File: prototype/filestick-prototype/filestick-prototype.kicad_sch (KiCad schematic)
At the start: 50 parts, among them U2 LMV324

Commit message: add GPIO headers etc
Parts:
- removed J?: Conn_01x07_Male, symbol Connector:Conn_01x07_Male
- added J3: GPIO header 1, symbol Connector:Conn_01x09_Male
- added J5: GPIO header 2, symbol Connector:Conn_01x16_Male
- added J6: SPI header, symbol Connector:Conn_01x10_Male
- added TP2: Econet TP header, symbol Connector:Conn_01x12_Male
- J4: renamed from J?; value Conn_01x05_Male -> UART header
- gave numbers to parts that had none: 47
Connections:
- net +3.3V: now also J3.1 (Pin_1), J5.16 (Pin_16), J6.10 (Pin_10), TP2.1 (Pin_1)
- net COLLISION_DETECT: now also TP2.2 (Pin_2)
- net COLLISION_REF_PWM: now also TP2.4 (Pin_4)
- net ECONET_CLKEN: now also TP2.10 (Pin_10)
- net ECONET_CLKIO: now also TP2.6 (Pin_6)
- net ECONET_RXD: now also TP2.7 (Pin_7)
- net ECONET_TXD: now also TP2.8 (Pin_8)
- net ECONET_TXEN: now also TP2.9 (Pin_9)
- net GND: now also J3.9 (Pin_9), J5.1 (Pin_1), J6.1 (Pin_1), TP2.12 (Pin_12)
- net TERM_EN: now also TP2.3 (Pin_3)
- net at U4.11 (GPIO23): now also J3.7 (Pin_7)
- net at U4.12 (GPIO25): now also J3.8 (Pin_8)
- net at U4.18 (GPIO37_G1): now also TP2.5 (Pin_5)
- net at U4.2 (VIO): now also J3.2 (Pin_2)
- net at U4.24 (GPIO28): now also TP2.11 (Pin_11)
- net at U4.25 (GPIO2): now also J5.2 (Pin_2)
- net at U4.26 (GPIO46): now also J5.3 (Pin_3)
- net at U4.27 (GPIO47): now also J5.4 (Pin_4)
- net at U4.28 (GPIO45): now also J5.5 (Pin_5)
- net at U4.29 (GPIO48): now also J5.6 (Pin_6)
- net at U4.30 (GPIO3): now also J5.7 (Pin_7)
- net at U4.31 (GPIO4): now also J5.8 (Pin_8)
- net at U4.32 (GPIO44_G6): now also J5.9 (Pin_9)
- net at U4.33 (GPIO6): now also J5.10 (Pin_10)
- net at U4.34 (GPIO9): now also J5.11 (Pin_11)
- net at U4.35 (GPIO11): now also J5.12 (Pin_12)
- net at U4.36 (GPIO18): now also J5.13 (Pin_13)
- net at U4.37 (GPIO19): now also J5.14 (Pin_14)
- net SD_CD: now reaches R17.2, U4.38 (GPIO13), U5.7 (CD)
- net SD_CD: now also J6.2 (Pin_2)
- net SS3: now reaches U4.39 (GPIO21_SS3)
- net SS3: now also J6.3 (Pin_3)
- net at U4.4 (CDONE): now also J3.3 (Pin_3)
- net SS2: now reaches U4.40 (GPIO12_SS2)
- net SS2: now also J6.4 (Pin_4)
- net SD_SS: now reaches U4.43 (GPIO10_SS1), U5.6 (/CS)
- net SD_SS: now also J6.5 (Pin_5)
- net GPIO_20: now reaches U4.44 (GPIO20_G3)
- net GPIO_20: now also J5.15 (Pin_15)
- net MOSI: now reaches U4.45 (GPIO14_MOSI), U5.3 (DI)
- net MOSI: now also J6.6 (Pin_6)
- net MISO: now reaches U4.46 (GPIO17_MISO), U5.4 (DO)
- net MISO: now also J6.7 (Pin_7)
- net SCK: now reaches U4.47 (GPIO15_SCK), U5.5 (SCLK)
- net SCK: now also J6.8 (Pin_8)
- net FLASH_SS: now reaches U4.48 (GPIO16_SS0)
- net FLASH_SS: now also J6.9 (Pin_9)
- net at U4.5 (GPIO41_RGB2): now also J3.4 (Pin_4)
- net at U4.6 (GPIO39_RGB0): now also J3.5 (Pin_5)
- net at U4.7 (GPIO40_RGB1): now also J3.6 (Pin_6)

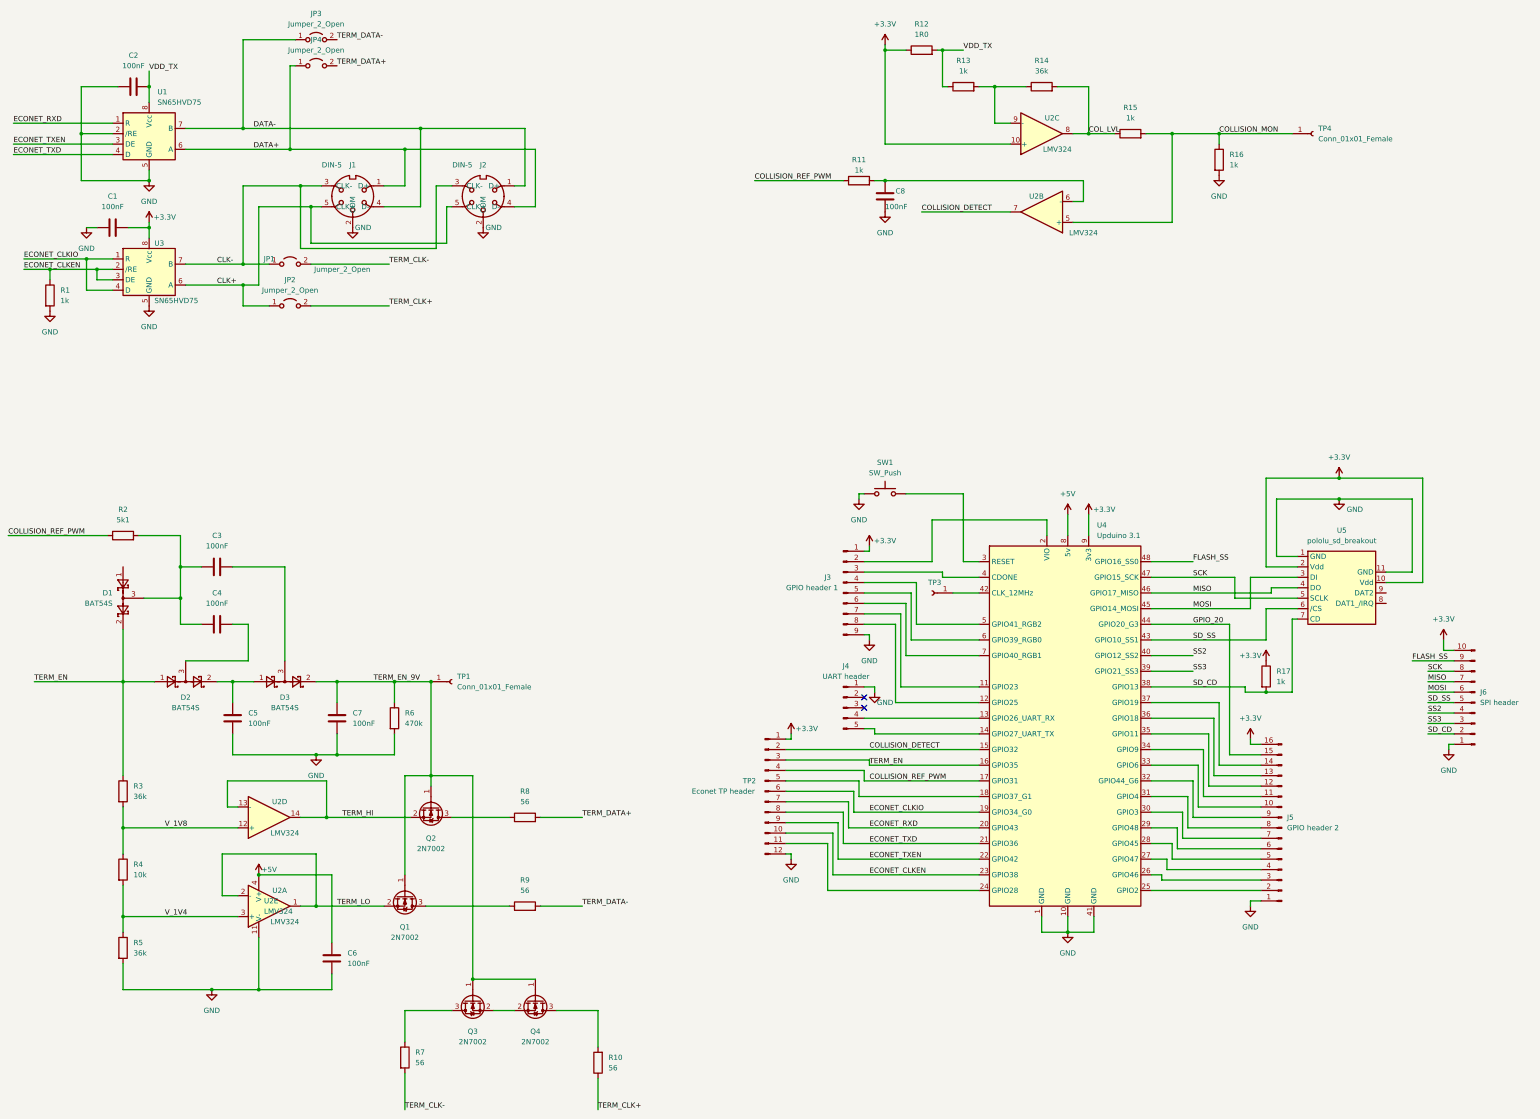
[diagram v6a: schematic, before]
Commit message: add annotations and footprints
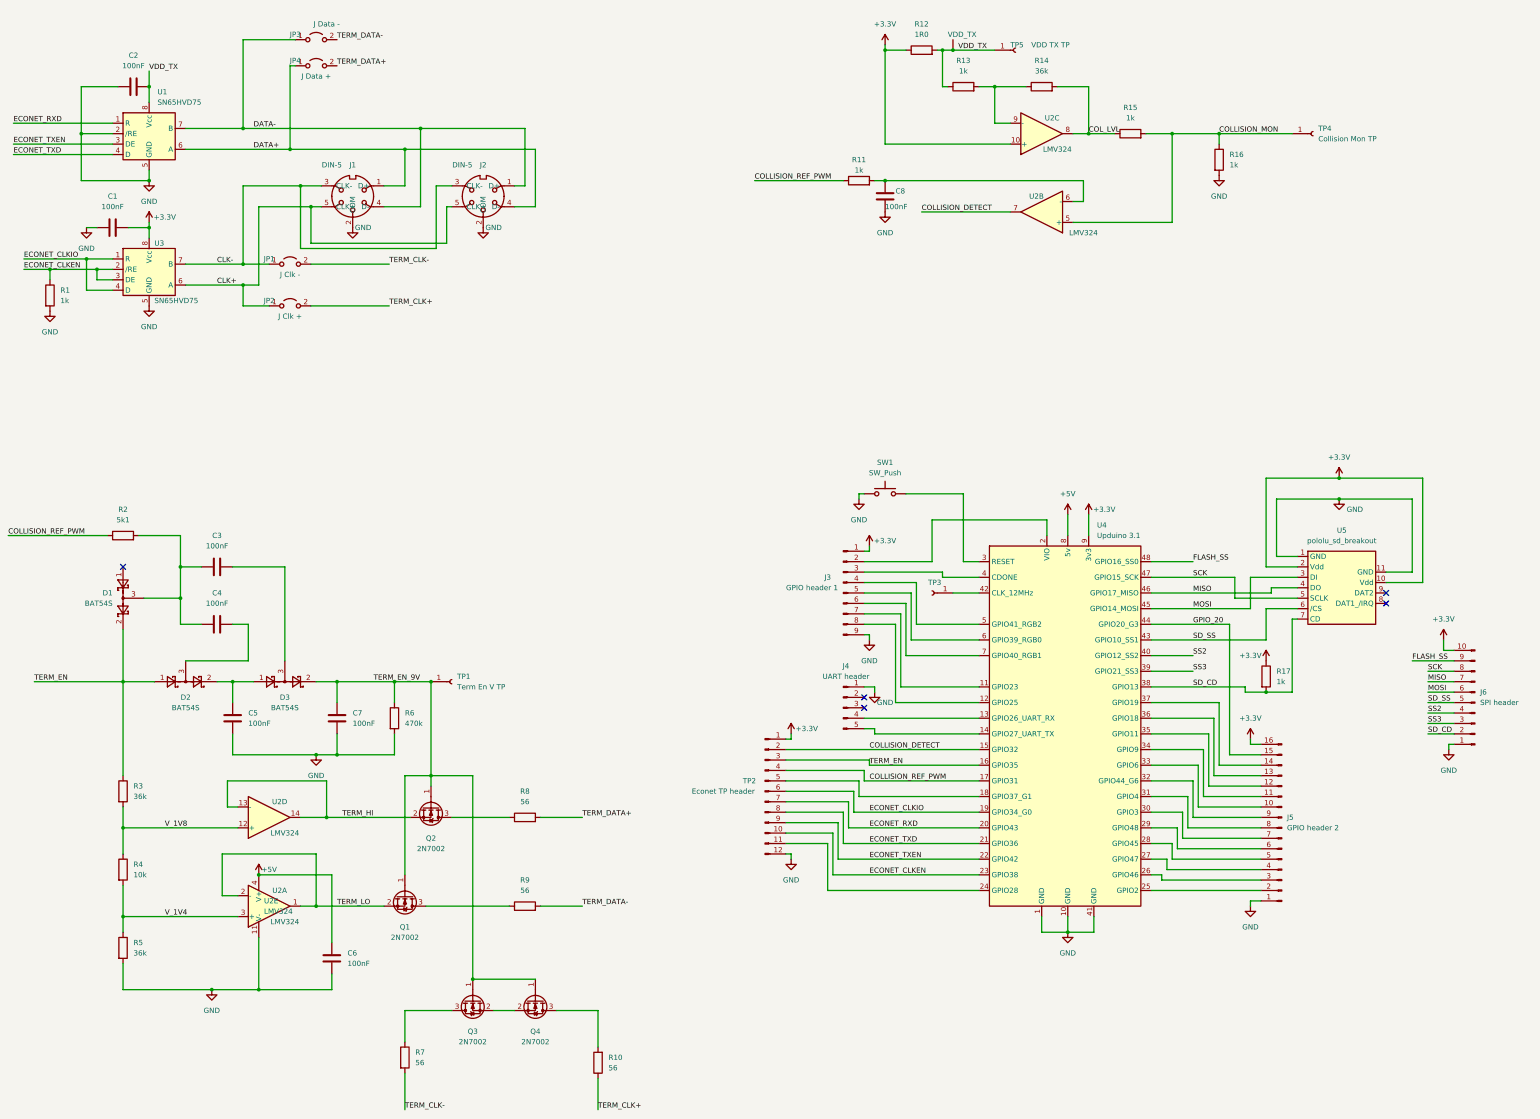
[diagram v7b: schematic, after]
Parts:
- added TP5: VDD TX TP, Connector_PinHeader_2.54mm:PinHeader_1x01_P2.54mm_Vertical, symbol Connector:Conn_01x01_Female
- C1, C2, C3, C4, C5, C6, C7, C8: footprint (none) -> Capacitor_SMD:C_0603_1608Metric_Pad1.08x0.95mm_HandSolder
- J1, J2: footprint (none) -> filestick-footprints:Lumberg_DIN41524_5pin
- J3: footprint (none) -> Connector_PinHeader_2.54mm:PinHeader_1x09_P2.54mm_Vertical
- J4: footprint (none) -> Connector_PinHeader_2.54mm:PinHeader_1x05_P2.54mm_Vertical
- J5: footprint (none) -> Connector_PinHeader_2.54mm:PinHeader_1x16_P2.54mm_Vertical
- J6: footprint (none) -> Connector_PinHeader_2.54mm:PinHeader_1x10_P2.54mm_Vertical
- JP1: value Jumper_2_Open -> J Clk -; footprint (none) -> Connector_PinHeader_2.54mm:PinHeader_1x02_P2.54mm_Vertical
- JP2: value Jumper_2_Open -> J Clk +; footprint (none) -> Connector_PinHeader_2.54mm:PinHeader_1x02_P2.54mm_Vertical
- JP3: value Jumper_2_Open -> J Data -; footprint (none) -> Connector_PinHeader_2.54mm:PinHeader_1x02_P2.54mm_Vertical
- JP4: value Jumper_2_Open -> J Data +; footprint (none) -> Connector_PinHeader_2.54mm:PinHeader_1x02_P2.54mm_Vertical
- R1, R10, R11, R12, R13, R14, R15, R16, R2, R3, R4, R5, R6, R7, R8, R9: footprint (none) -> Resistor_SMD:R_0603_1608Metric_Pad0.98x0.95mm_HandSolder
- TP1: value Conn_01x01_Female -> Term En V TP; footprint (none) -> Connector_PinHeader_2.54mm:PinHeader_1x01_P2.54mm_Vertical
- TP2: footprint (none) -> Connector_PinHeader_2.54mm:PinHeader_1x12_P2.54mm_Vertical
- TP4: value Conn_01x01_Female -> Collision Mon TP; footprint (none) -> Connector_PinHeader_2.54mm:PinHeader_1x01_P2.54mm_Vertical
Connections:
- net VDD_TX: now also TP5.1 (Pin_1)
- no-connect marks 2 -> 5

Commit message: More footprints
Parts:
- R17: footprint (none) -> Resistor_SMD:R_0603_1608Metric_Pad0.98x0.95mm_HandSolder
- SW1: footprint (none) -> Button_Switch_THT:SW_PUSH_6mm
- TP3: footprint (none) -> Connector_PinHeader_2.54mm:PinHeader_1x01_P2.54mm_Vertical
- U2: footprint (none) -> Package_SO:SOIC-14_3.9x8.7mm_P1.27mm
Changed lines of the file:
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@@
     (property "Reference" "SW1" (id 0) (at 227.33 127 0))
     (property "Value" "SW_Push" (id 1) (at 227.33 129.54 0))
-    (property "Footprint" "" (id 2) (at 227.33 129.54 0)
+    (property "Footprint" "Button_Switch_THT:SW_PUSH_6mm" (id 2) (at 227.33 129.54 0)
       (effects (font (size 1.27 1.27)) hide)
     )
@@
     (property "Reference" "U2" (id 0) (at 267.97 43.18 0))
     (property "Value" "LMV324" (id 1) (at 269.24 50.8 0))
-    (property "Footprint" "" (id 2) (at 264.16 49.53 0)
+    (property "Footprint" "Package_SO:SOIC-14_3.9x8.7mm_P1.27mm" (id 2) (at 264.16 49.53 0)
       (effects (font (size 1.27 1.27)) hide)
     )
@@
       (effects (font (size 1.27 1.27)) hide)
     )
-    (property "Footprint" "" (id 2) (at 238.76 158.75 0)
+    (property "Footprint" "Connector_PinHeader_2.54mm:PinHeader_1x01_P2.54mm_Vertical" (id 2) (at 238.76 158.75 0)
       (effects (font (size 1.27 1.27)) hide)
     )
@@
       (effects (font (size 1.27 1.27)) (justify left))
     )
-    (property "Footprint" "" (id 2) (at 76.2 232.41 0)
+    (property "Footprint" "Package_SO:SOIC-14_3.9x8.7mm_P1.27mm" (id 2) (at 76.2 232.41 0)
       (effects (font (size 1.27 1.27)) hide)
     )
@@
       (effects (font (size 1.27 1.27)) (justify left))
     )
-    (property "Footprint" "" (id 2) (at 318.262 179.07 90)
+    (property "Footprint" "Resistor_SMD:R_0603_1608Metric_Pad0.98x0.95mm_HandSolder" (id 2) (at 318.262 179.07 90)
       (effects (font (size 1.27 1.27)) hide)
     )
@@
     (property "Reference" "U2" (id 0) (at 80.01 209.55 0))
     (property "Value" "LMV324" (id 1) (at 81.28 217.17 0))
-    (property "Footprint" "" (id 2) (at 76.2 215.9 0)
+    (property "Footprint" "Package_SO:SOIC-14_3.9x8.7mm_P1.27mm" (id 2) (at 76.2 215.9 0)
       (effects (font (size 1.27 1.27)) hide)
     )
@@
     (property "Reference" "U2" (id 0) (at 80.01 231.14 0))
     (property "Value" "LMV324" (id 1) (at 81.28 238.76 0))
-    (property "Footprint" "" (id 2) (at 76.2 237.49 0)
+    (property "Footprint" "Package_SO:SOIC-14_3.9x8.7mm_P1.27mm" (id 2) (at 76.2 237.49 0)
       (effects (font (size 1.27 1.27)) hide)
     )
@@
     (property "Reference" "U2" (id 0) (at 264.16 62.23 0))
     (property "Value" "LMV324" (id 1) (at 275.59 71.12 0))
-    (property "Footprint" "" (id 2) (at 266.7 68.58 0)
+    (property "Footprint" "Package_SO:SOIC-14_3.9x8.7mm_P1.27mm" (id 2) (at 266.7 68.58 0)
       (effects (font (size 1.27 1.27)) hide)
     )
@@
     )
     (path "/9ad6df3f-ebe7-46e6-a4e7-9fe34543eb2c"
-      (reference "R17") (unit 1) (value "1k") (footprint "")
+      (reference "R17") (unit 1) (value "1k") (footprint "Resistor_SMD:R_0603_1608Metric_Pad0.98x0.95mm_HandSolder")
     )
     (path "/15050c23-4fd9-40f6-936a-a24056cc4858"
-      (reference "SW1") (unit 1) (value "SW_Push") (footprint "")
+      (reference "SW1") (unit 1) (value "SW_Push") (footprint "Button_Switch_THT:SW_PUSH_6mm")
     )
     (path "/fdec3421-c7db-441a-bb89-5d9ad1a7c793"
@@
     )
     (path "/33eae399-3758-4dd2-a201-b21025de9dac"
-      (reference "TP3") (unit 1) (value "Conn_01x01_Female") (footprint "")
+      (reference "TP3") (unit 1) (value "Conn_01x01_Female") (footprint "Connector_PinHeader_2.54mm:PinHeader_1x01_P2.54mm_Vertical")
     )
     (path "/c7ba7277-528a-472f-9745-810713900589"
@@
     )
     (path "/b19894d5-7fa9-4eca-8f7f-504f876287db"
-      (reference "U2") (unit 1) (value "LMV324") (footprint "")
+      (reference "U2") (unit 1) (value "LMV324") (footprint "Package_SO:SOIC-14_3.9x8.7mm_P1.27mm")
     )
     (path "/c8d9109f-29ec-4dcc-8afa-923b80be6987"
-      (reference "U2") (unit 2) (value "LMV324") (footprint "")
+      (reference "U2") (unit 2) (value "LMV324") (footprint "Package_SO:SOIC-14_3.9x8.7mm_P1.27mm")
     )
     (path "/32f44d8e-aa46-4c1f-b9ba-55ec78a09e8c"
-      (reference "U2") (unit 3) (value "LMV324") (footprint "")
+      (reference "U2") (unit 3) (value "LMV324") (footprint "Package_SO:SOIC-14_3.9x8.7mm_P1.27mm")
     )
     (path "/b06ce78a-852b-4fdf-ad38-fd7516f708ba"
-      (reference "U2") (unit 4) (value "LMV324") (footprint "")
+      (reference "U2") (unit 4) (value "LMV324") (footprint "Package_SO:SOIC-14_3.9x8.7mm_P1.27mm")
     )
     (path "/47163286-6007-4ebb-9ba0-6b76e2eec328"
-      (reference "U2") (unit 5) (value "LMV324") (footprint "")
+      (reference "U2") (unit 5) (value "LMV324") (footprint "Package_SO:SOIC-14_3.9x8.7mm_P1.27mm")
     )
     (path "/729fac80-7f4c-4077-9d0c-4f5f4f39b6ed"
